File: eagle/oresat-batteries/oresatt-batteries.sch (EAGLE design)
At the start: 4 parts

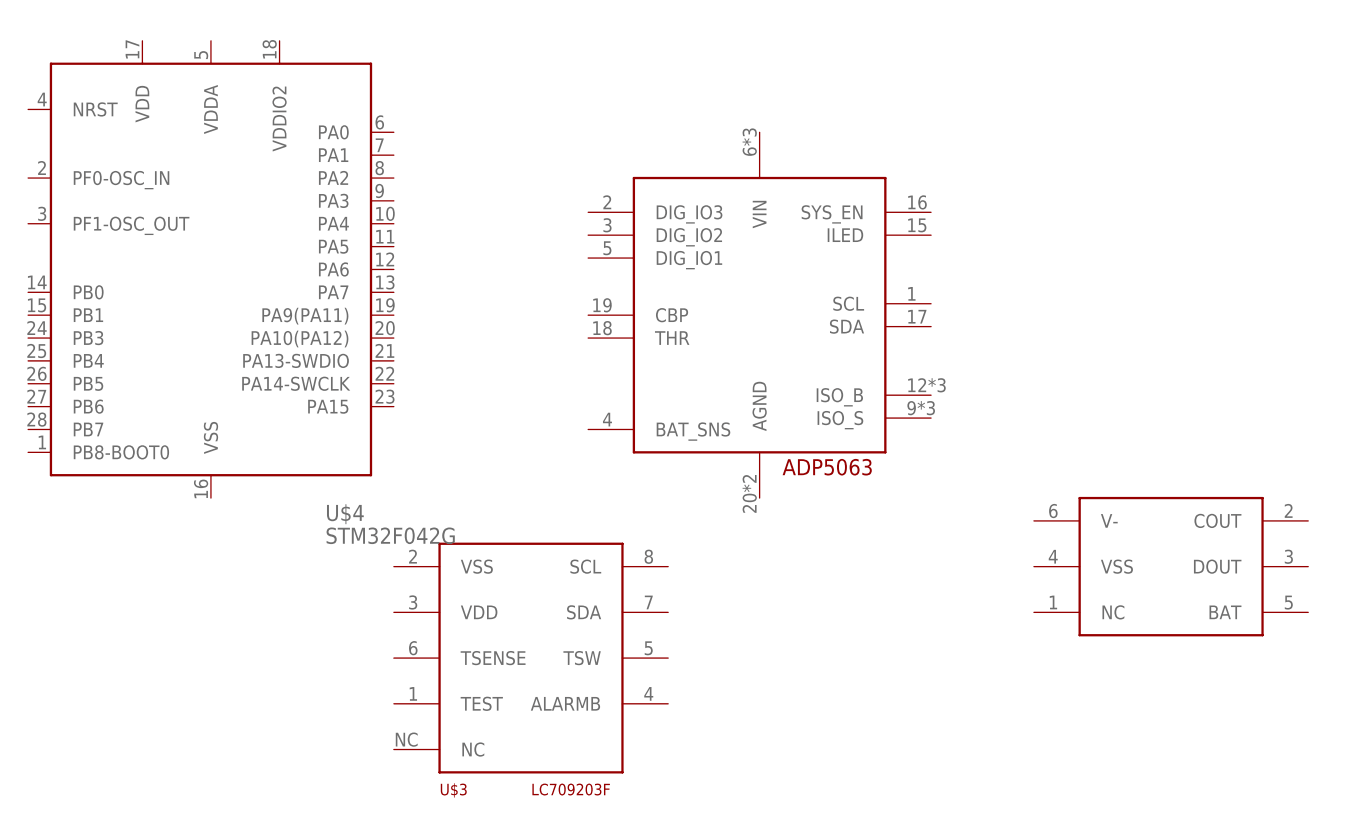
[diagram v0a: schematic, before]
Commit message: Added crystal, CAN transciever
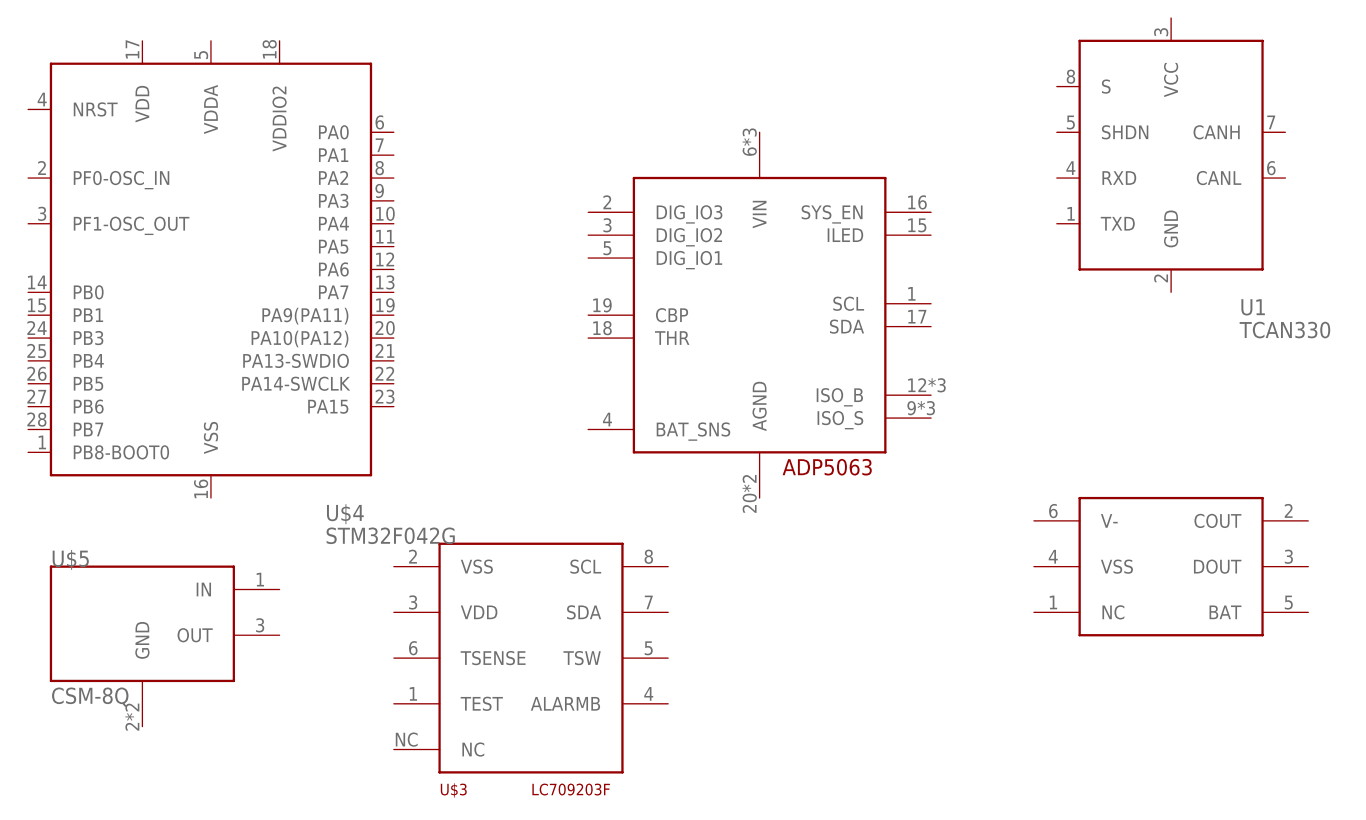
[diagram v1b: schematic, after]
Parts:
- added U$5: CSM-8Q, oresat-batteries:CSM-8Q
- added U1: TCAN330, oresat-batteries:TCAN330
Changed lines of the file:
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@@
 <part name="U$3" library="oresat-batteries" deviceset="LC709203F" device=""/>
 <part name="U$4" library="oresat-batteries" deviceset="STM32F042G" device=""/>
+<part name="U$5" library="oresat-batteries" deviceset="CSM-8Q" device=""/>
+<part name="U1" library="oresat-batteries" deviceset="TCAN330" device=""/>
 </parts>
 <sheets>
@@
 <instance part="U$3" gate="G$1" x="-25.4" y="-38.1"/>
 <instance part="U$4" gate="G$1" x="-60.96" y="5.08"/>
+<instance part="U$5" gate="G$1" x="-68.58" y="-33.02"/>
+<instance part="U1" gate="G$1" x="45.72" y="17.78"/>
 </instances>
 <busses>

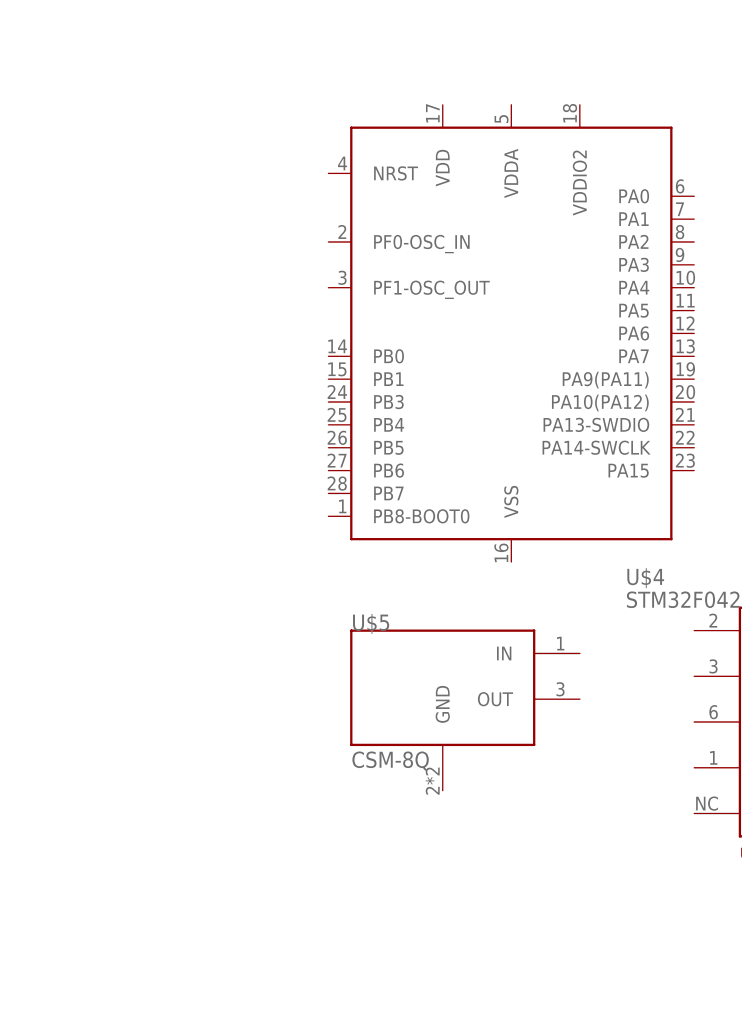
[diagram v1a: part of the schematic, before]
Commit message: Changed board to real max dimensions.  Added 40pin connector
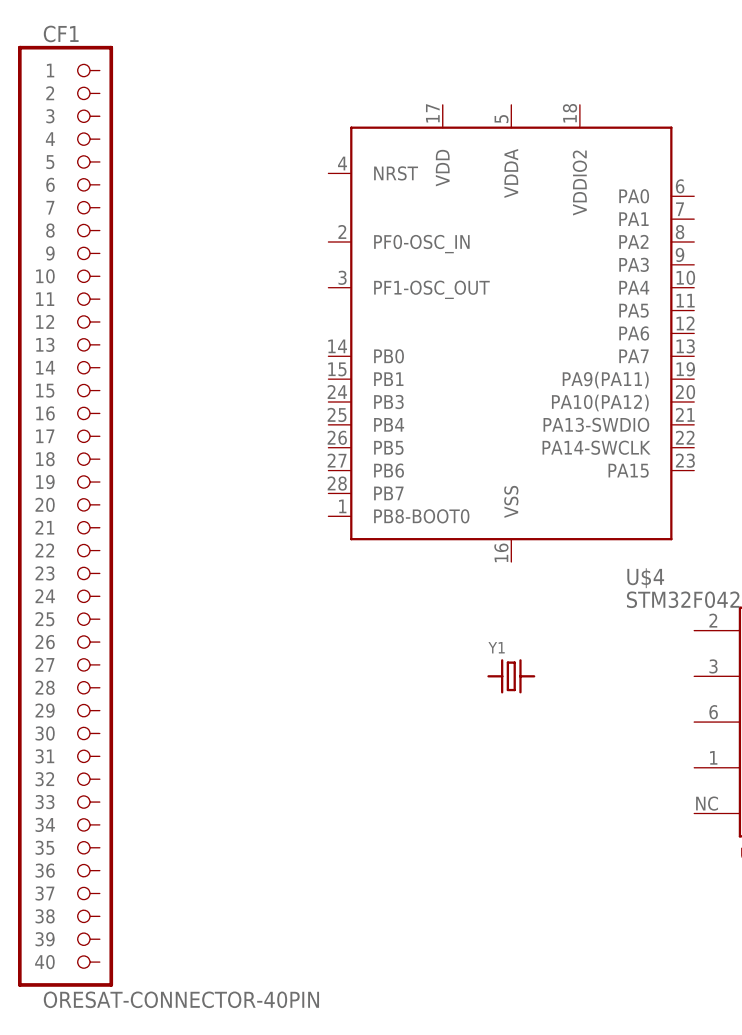
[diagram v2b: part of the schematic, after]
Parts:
- removed U$5: CSM-8Q, oresat-batteries:CSM-8Q
- added CF1: ORESAT-CONNECTOR-40PIN, low-gain-radio:ORESAT-CONNECTOR-40PIN
- added Y1: (no value), low-gain-radio:CRYSTAL2.5X2.0MM
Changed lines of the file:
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@@
 <layer number="48" name="Document" color="7" fill="1" visible="no" active="no"/>
 <layer number="49" name="Reference" color="7" fill="1" visible="no" active="no"/>
+<layer number="50" name="dxf" color="7" fill="1" visible="no" active="no"/>
 <layer number="51" name="tDocu" color="7" fill="1" visible="no" active="no"/>
 <layer number="52" name="bDocu" color="7" fill="1" visible="no" active="no"/>
+<layer number="53" name="tGND_GNDA" color="7" fill="1" visible="no" active="no"/>
+<layer number="54" name="bGND_GNDA" color="7" fill="1" visible="no" active="no"/>
+<layer number="56" name="wert" color="7" fill="1" visible="no" active="no"/>
+<layer number="57" name="tCAD" color="7" fill="1" visible="no" active="no"/>
+<layer number="58" name="b3D" color="7" fill="1" visible="no" active="no"/>
+<layer number="59" name="Invisible" color="7" fill="1" visible="no" active="no"/>
+<layer number="61" name="stand" color="7" fill="1" visible="no" active="no"/>
 <layer number="90" name="Modules" color="5" fill="1" visible="yes" active="yes"/>
 <layer number="91" name="Nets" color="2" fill="1" visible="yes" active="yes"/>
@@
 <layer number="97" name="Info" color="7" fill="1" visible="yes" active="yes"/>
 <layer number="98" name="Guide" color="6" fill="1" visible="yes" active="yes"/>
+<layer number="99" name="SpiceOrder" color="7" fill="1" visible="yes" active="yes"/>
+<layer number="100" name="TODO" color="7" fill="1" visible="yes" active="yes"/>
+<layer number="101" name="Hidden" color="7" fill="1" visible="yes" active="yes"/>
+<layer number="102" name="Changes" color="7" fill="1" visible="yes" active="yes"/>
+<layer number="103" name="tMap" color="7" fill="1" visible="yes" active="yes"/>
+<layer number="104" name="Name" color="7" fill="1" visible="yes" active="yes"/>
+<layer number="105" name="Beschreib" color="7" fill="1" visible="yes" active="yes"/>
+<layer number="106" name="BGA-Top" color="7" fill="1" visible="yes" active="yes"/>
+<layer number="107" name="BD-Top" color="7" fill="1" visible="yes" active="yes"/>
+<layer number="108" name="tplace-old" color="7" fill="1" visible="yes" active="yes"/>
+<layer number="109" name="ref-old" color="7" fill="1" visible="yes" active="yes"/>
+<layer number="110" name="fp0" color="7" fill="1" visible="yes" active="yes"/>
+<layer number="111" name="LPC17xx" color="7" fill="1" visible="yes" active="yes"/>
+<layer number="112" name="tSilk" color="7" fill="1" visible="yes" active="yes"/>
+<layer number="113" name="ReferenceLS" color="7" fill="1" visible="yes" active="yes"/>
+<layer number="114" name="secv1" color="7" fill="1" visible="yes" active="yes"/>
+<layer number="115" name="secv12" color="7" fill="1" visible="yes" active="yes"/>
+<layer number="116" name="Patch_BOT" color="7" fill="1" visible="yes" active="yes"/>
+<layer number="117" name="secv21" color="7" fill="1" visible="yes" active="yes"/>
+<layer number="118" name="Rect_Pads" color="7" fill="1" visible="yes" active="yes"/>
+<layer number="121" name="_tsilk" color="7" fill="1" visible="yes" active="yes"/>
+<layer number="122" name="_bsilk" color="7" fill="1" visible="yes" active="yes"/>
+<layer number="123" name="tTestmark" color="7" fill="1" visible="yes" active="yes"/>
+<layer number="124" name="bTestmark" color="7" fill="1" visible="yes" active="yes"/>
+<layer number="125" name="_tNames" color="7" fill="1" visible="yes" active="yes"/>
+<layer number="126" name="_bNames" color="7" fill="1" visible="yes" active="yes"/>
+<layer number="127" name="_tValues" color="7" fill="1" visible="yes" active="yes"/>
+<layer number="128" name="_bValues" color="7" fill="1" visible="yes" active="yes"/>
+<layer number="130" name="bLogo" color="7" fill="1" visible="yes" active="yes"/>
+<layer number="131" name="tAdjust" color="7" fill="1" visible="yes" active="yes"/>
+<layer number="132" name="bAdjust" color="7" fill="1" visible="yes" active="yes"/>
+<layer number="144" name="Drill_legend" color="7" fill="1" visible="yes" active="yes"/>
+<layer number="150" name="Notes" color="7" fill="1" visible="yes" active="yes"/>
+<layer number="151" name="HeatSink" color="7" fill="1" visible="yes" active="yes"/>
+<layer number="152" name="_bDocu" color="7" fill="1" visible="yes" active="yes"/>
+<layer number="153" name="FabDoc1" color="7" fill="1" visible="yes" active="yes"/>
+<layer number="154" name="FabDoc2" color="7" fill="1" visible="yes" active="yes"/>
+<layer number="155" name="FabDoc3" color="7" fill="1" visible="yes" active="yes"/>
+<layer number="199" name="Contour" color="7" fill="1" visible="yes" active="yes"/>
+<layer number="200" name="200bmp" color="7" fill="1" visible="yes" active="yes"/>
+<layer number="201" name="201bmp" color="7" fill="1" visible="yes" active="yes"/>
+<layer number="202" name="202bmp" color="7" fill="1" visible="yes" active="yes"/>
+<layer number="203" name="203bmp" color="7" fill="1" visible="yes" active="yes"/>
+<layer number="204" name="204bmp" color="7" fill="1" visible="yes" active="yes"/>
+<layer number="205" name="205bmp" color="7" fill="1" visible="yes" active="yes"/>
+<layer number="206" name="206bmp" color="7" fill="1" visible="yes" active="yes"/>
+<layer number="207" name="207bmp" color="7" fill="1" visible="yes" active="yes"/>
+<layer number="208" name="208bmp" color="7" fill="1" visible="yes" active="yes"/>
+<layer number="209" name="209bmp" color="7" fill="1" visible="yes" active="yes"/>
+<layer number="210" name="210bmp" color="7" fill="1" visible="yes" active="yes"/>
+<layer number="211" name="211bmp" color="7" fill="1" visible="yes" active="yes"/>
+<layer number="212" name="212bmp" color="7" fill="1" visible="yes" active="yes"/>
+<layer number="213" name="213bmp" color="7" fill="1" visible="yes" active="yes"/>
+<layer number="214" name="214bmp" color="7" fill="1" visible="yes" active="yes"/>
+<layer number="215" name="215bmp" color="7" fill="1" visible="yes" active="yes"/>
+<layer number="216" name="216bmp" color="7" fill="1" visible="yes" active="yes"/>
+<layer number="217" name="217bmp" color="7" fill="1" visible="yes" active="yes"/>
+<layer number="218" name="218bmp" color="7" fill="1" visible="yes" active="yes"/>
+<layer number="219" name="219bmp" color="7" fill="1" visible="yes" active="yes"/>
+<layer number="220" name="220bmp" color="7" fill="1" visible="yes" active="yes"/>
+<layer number="221" name="221bmp" color="7" fill="1" visible="yes" active="yes"/>
+<layer number="222" name="222bmp" color="7" fill="1" visible="yes" active="yes"/>
+<layer number="223" name="223bmp" color="7" fill="1" visible="yes" active="yes"/>
+<layer number="224" name="224bmp" color="7" fill="1" visible="yes" active="yes"/>
+<layer number="225" name="225bmp" color="7" fill="1" visible="yes" active="yes"/>
+<layer number="226" name="226bmp" color="7" fill="1" visible="yes" active="yes"/>
+<layer number="227" name="227bmp" color="7" fill="1" visible="yes" active="yes"/>
+<layer number="228" name="228bmp" color="7" fill="1" visible="yes" active="yes"/>
+<layer number="231" name="Eagle3D_PG1" color="7" fill="1" visible="yes" active="yes"/>
+<layer number="232" name="Eagle3D_PG2" color="7" fill="1" visible="yes" active="yes"/>
+<layer number="233" name="Eagle3D_PG3" color="7" fill="1" visible="yes" active="yes"/>
+<layer number="248" name="Housing" color="7" fill="1" visible="yes" active="yes"/>
+<layer number="249" name="Edge" color="7" fill="1" visible="yes" active="yes"/>
+<layer number="250" name="Descript" color="7" fill="1" visible="yes" active="yes"/>
+<layer number="251" name="SMDround" color="7" fill="1" visible="yes" active="yes"/>
+<layer number="254" name="cooling" color="7" fill="1" visible="yes" active="yes"/>
 </layers>
 <schematic xreflabel="%F%N/%S.%C%R" xrefpart="/%S.%C%R">
@@
 <part name="U$3" library="oresat-batteries" deviceset="LC709203F" device=""/>
 <part name="U$4" library="oresat-batteries" deviceset="STM32F042G" device=""/>
-<part name="U$5" library="oresat-batteries" deviceset="CSM-8Q" device=""/>
 <part name="U1" library="oresat-batteries" deviceset="TCAN330" device=""/>
+<part name="Y1" library="low-gain-radio" deviceset="CRYSTAL" device="2.5X2.0MM"/>
+<part name="CF1" library="low-gain-radio" deviceset="ORESAT-CONNECTOR-40PIN" device=""/>
 </parts>
 <sheets>
@@
 <instance part="U$3" gate="G$1" x="-25.4" y="-38.1"/>
 <instance part="U$4" gate="G$1" x="-60.96" y="5.08"/>
-<instance part="U$5" gate="G$1" x="-68.58" y="-33.02"/>
 <instance part="U1" gate="G$1" x="45.72" y="17.78"/>
+<instance part="Y1" gate="G$1" x="-60.96" y="-33.02"/>
+<instance part="CF1" gate="G$1" x="-106.68" y="-15.24"/>
 </instances>
 <busses>

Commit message: Removed locks!
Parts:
- removed CF1: ORESAT-CONNECTOR-40PIN, low-gain-radio:ORESAT-CONNECTOR-40PIN
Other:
- moved on the sheet: Y1
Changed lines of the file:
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@@
 <part name="U1" library="oresat-batteries" deviceset="TCAN330" device=""/>
 <part name="Y1" library="low-gain-radio" deviceset="CRYSTAL" device="2.5X2.0MM"/>
-<part name="CF1" library="low-gain-radio" deviceset="ORESAT-CONNECTOR-40PIN" device=""/>
 </parts>
 <sheets>
@@
 <instance part="U$4" gate="G$1" x="-60.96" y="5.08"/>
 <instance part="U1" gate="G$1" x="45.72" y="17.78"/>
-<instance part="Y1" gate="G$1" x="-60.96" y="-33.02"/>
-<instance part="CF1" gate="G$1" x="-106.68" y="-15.24"/>
+<instance part="Y1" gate="G$1" x="-73.66" y="-38.1"/>
 </instances>
 <busses>
